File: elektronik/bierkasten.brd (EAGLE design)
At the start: 41 x 51 mm, 81 parts, among them Q1 BC547B, Q2 NXP2301P-SOT23

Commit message: Fertigungsdaten erstellt
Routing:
- net !RESET: track 52.9 -> 52.1 mm
- net GND: vias 37 -> 38
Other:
- board text added: "B.Cool v 1.0"
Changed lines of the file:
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@@
 <circle x="37.5" y="47" radius="3.2" width="0.2" layer="42"/>
 <hole x="37.5" y="47" drill="3.4"/>
+<text x="6.6" y="30.8" size="1.778" layer="1" font="vector" ratio="10">B.Cool
+v 1.0</text>
+<wire x1="13.4" y1="33.4" x2="12.2" y2="32.2" width="0.2" layer="41"/>
+<wire x1="12.2" y1="32.2" x2="12.2" y2="31.2" width="0.2" layer="41"/>
+<wire x1="12.2" y1="31.2" x2="11.8" y2="30.6" width="0.2" layer="41"/>
+<wire x1="11.8" y1="30.6" x2="11.2" y2="30.6" width="0.2" layer="41"/>
+<wire x1="11.2" y1="30.6" x2="6.4" y2="30.6" width="0.2" layer="41"/>
+<wire x1="6.4" y1="30.6" x2="6.4" y2="35.4" width="0.2" layer="41"/>
+<wire x1="6.4" y1="35.4" x2="13.4" y2="35.4" width="0.2" layer="41"/>
+<wire x1="13.4" y1="35.4" x2="13.4" y2="33.4" width="0.2" layer="41"/>
 </plain>
 <attributes>
@@
 <element name="TA1" library="switch_STE" package="TA93XX" value="KURZHUBTASTER" x="6.6" y="39.8" rot="R180">
 <attribute name="FARNELL" value="2292960" x="6.6" y="39.8" size="1.778" layer="27" rot="R180" display="off"/>
-<attribute name="REICHELT" value="Taster 9314" x="6.6" y="39.8" size="1.778" layer="27" rot="R180" display="off"/>
-<attribute name="WUERTH" value="430 182 043 816" x="6.6" y="39.8" size="1.778" layer="27" rot="R180" display="off"/>
 </element>
 <element name="U$15" library="misc_STE" package="ESP8266-POLLIN" value="ESP8266-POLLIN" x="14.8" y="18.4" rot="R90">
@@
 <attribute name="REICHELT" value="NX2301P NXP" x="12.4" y="6.4" size="1.778" layer="28" rot="MR270" display="off"/>
 </element>
-<element name="R28" library="rcl" library_urn="urn:adsk.eagle:library:334" package="R0603" package3d_urn="urn:adsk.eagle:package:23555/2" value="10k" x="14.8" y="6.4" rot="MR270">
+<element name="R28" library="rcl" library_urn="urn:adsk.eagle:library:334" package="R0603" package3d_urn="urn:adsk.eagle:package:23555/2" value="10k" x="14.8" y="6.4" smashed="yes" rot="MR270">
 <attribute name="FARNELL" value="2502397" x="14.8" y="6.4" size="1.778" layer="28" rot="MR270" display="off"/>
+<attribute name="NAME" x="14.165" y="7.035" size="1.27" layer="26" rot="MR270"/>
 <attribute name="REICHELT" value="RND 0603 1 10K" x="14.8" y="6.4" size="1.778" layer="28" rot="MR270" display="off"/>
 <attribute name="SPICEPREFIX" value="R" x="14.8" y="6.4" size="1.778" layer="28" rot="MR270" display="off"/>
+<attribute name="VALUE" x="16.705" y="7.035" size="1.27" layer="28" rot="MR270"/>
 </element>
 <element name="U$16" library="power_STE" package="SOT223" value="NCP1117ST33T3G" x="11.4" y="39" rot="MR90">
@@
 <via x="12.6" y="12.8" extent="1-16" drill="0.4"/>
 <via x="4" y="29.4" extent="1-16" drill="0.4"/>
-<via x="7" y="34.8" extent="1-16" drill="0.4"/>
+<via x="5.6" y="36.6" extent="1-16" drill="0.4"/>
 <via x="18.2" y="39.4" extent="1-16" drill="0.4"/>
-<via x="11.6" y="30.2" extent="1-16" drill="0.4"/>
+<via x="11.6" y="29.8" extent="1-16" drill="0.4"/>
 <via x="10.8" y="46.8" extent="1-16" drill="0.4"/>
-<via x="13.8" y="34" extent="1-16" drill="0.4"/>
+<via x="14.4" y="34" extent="1-16" drill="0.4"/>
 <via x="39.8" y="41.2" extent="1-16" drill="0.4"/>
 <via x="38.2" y="40.6" extent="1-16" drill="0.4"/>
@@
 <wire x1="40.45" y1="31.7" x2="34.65" y2="31.7" width="0.2" layer="16"/>
 <wire x1="40.4" y1="33.78" x2="34.6" y2="33.78" width="0.2" layer="16"/>
+<via x="9.6" y="15.2" extent="1-16" drill="0.4"/>
 </signal>
 <signal name="AVCC">
@@
 <wire x1="11.1524" y1="22.04065" x2="11.1524" y2="23.65455" width="0.2" layer="16"/>
 <wire x1="12.90455" y1="21.7976" x2="11.39545" y2="21.7976" width="0.2" layer="16"/>
-<wire x1="2.1" y1="42.05" x2="2.1" y2="42.4" width="0.2" layer="1"/>
-<wire x1="2.1" y1="42.4" x2="2.1" y2="42.5" width="0.2" layer="1"/>
 <wire x1="11.1" y1="42.05" x2="2.1" y2="42.05" width="0.2" layer="1"/>
 <wire x1="20.92" y1="42.05" x2="23.6" y2="44.73" width="0.2" layer="1"/>
@@
 <wire x1="11.6" y1="28" x2="10" y2="26.4" width="0.2" layer="16"/>
 <wire x1="10" y1="26.4" x2="10" y2="24.1976" width="0.2" layer="16"/>
-<wire x1="2.1" y1="42.05" x2="2.1" y2="42.4" width="0.2" layer="1"/>
 </signal>
 <signal name="N$1">
@@
 </drawing>
 <compatibility>
+<note version="6.3" minversion="6.2.2" severity="warning">
+Since Version 6.2.2 text objects can contain more than one line,
+which will not be processed correctly with this version.
+</note>
 <note version="8.2" severity="warning">
 Since Version 8.2, EAGLE supports online libraries. The ids

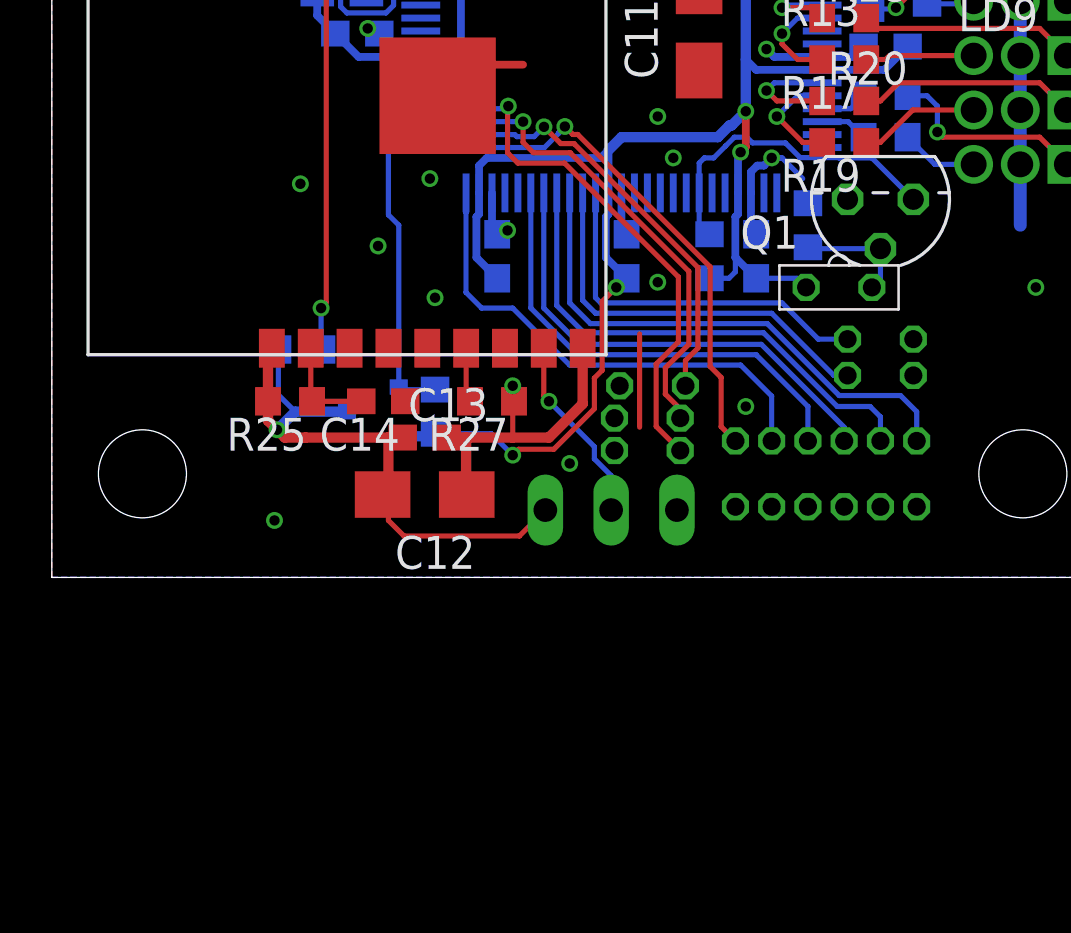
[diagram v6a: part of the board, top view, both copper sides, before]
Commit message: Light detection has its own PCB
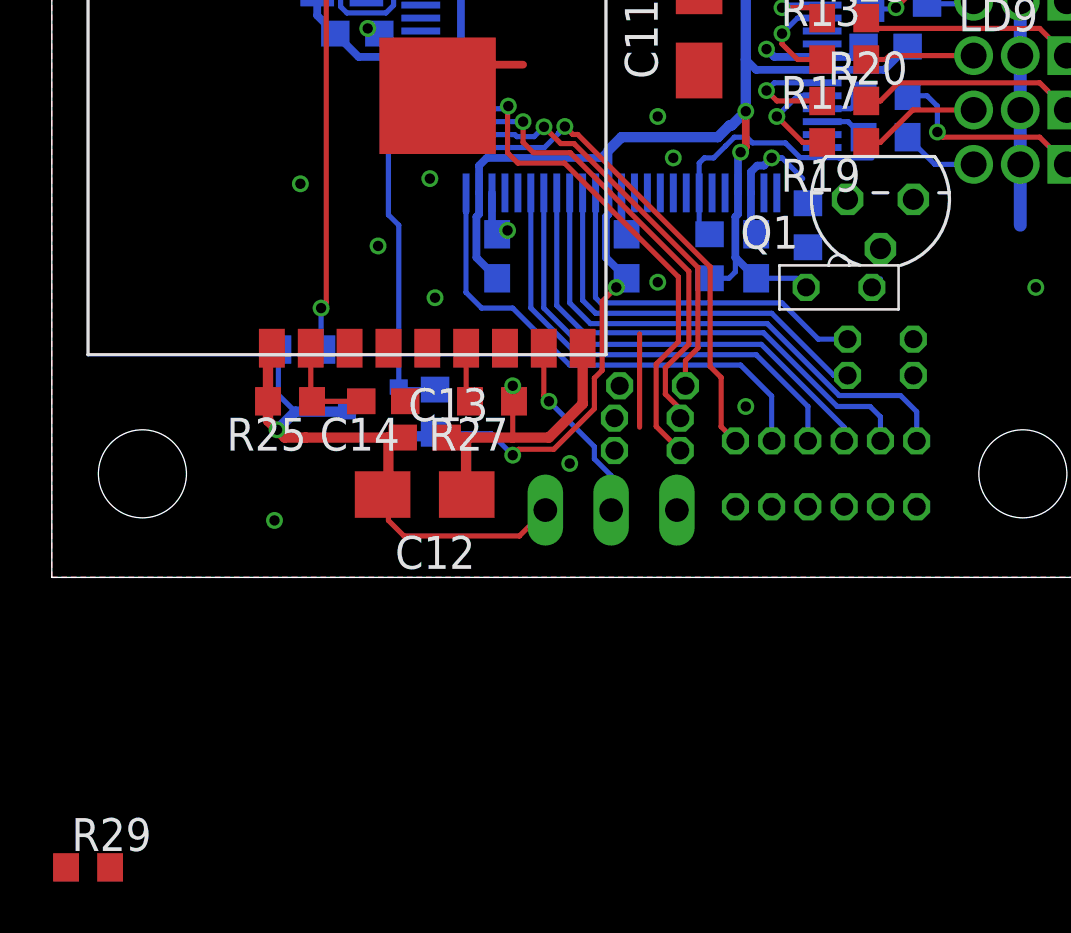
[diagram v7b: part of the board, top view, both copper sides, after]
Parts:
- added R29: 10k, rcl_STE:R0603
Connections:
- new net N$27: Q1.3
- new net N$28: Q1.2, R29.1
- net !LIGHT_ON: no longer Q1.3
- net N$23: now also R29.2; no longer Q1.2
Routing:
- net N$23: track 4.45 -> 0.54 mm
- net !LIGHT_ON: track 12.6 -> 10.3 mm
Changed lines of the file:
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@@
 <attribute name="SPICEPREFIX" value="C" x="3.4" y="39" size="1.778" layer="28" rot="MR90" display="off"/>
+</element>
+<element name="R29" library="rcl_STE" package="R0603" package3d_urn="urn:adsk.eagle:package:23555/2" value="10k" x="1.4" y="-11.2">
+<attribute name="REICHELT" value="RND 0603 1 1,0M" x="1.4" y="-11.2" size="1.778" layer="27" display="off"/>
+<attribute name="SPICEPREFIX" value="R" x="1.4" y="-11.2" size="1.778" layer="27" display="off"/>
 </element>
 </elements>
@@
 <contactref element="U$2" pad="4"/>
 <contactref element="R24" pad="2"/>
-<contactref element="U$3" pad="C"/>
 <wire x1="29.75" y1="24.6" x2="32.05" y2="24.6" width="0.3" layer="16"/>
 <wire x1="32.05" y1="24.6" x2="33.05" y2="25.6" width="0.3" layer="16"/>
@@
 <wire x1="26.3976" y1="11.7976" x2="26.15" y2="11.55" width="0.2" layer="16"/>
 <wire x1="27.2" y1="11.55" x2="28.78" y2="11.55" width="0.2" layer="16"/>
-<wire x1="28.78" y1="11.55" x2="29.13" y2="11.2" width="0.2" layer="16"/>
 <wire x1="10.625" y1="32.2" x2="10.45" y2="32.375" width="1" layer="16"/>
 <wire x1="10.45" y1="32.375" x2="10.45" y2="34.4" width="1" layer="16"/>
@@
 <wire x1="26.14" y1="42.0406" x2="26.14" y2="41.74" width="0.2" layer="1"/>
 <wire x1="24.6" y1="40.2" x2="30.8" y2="40.2" width="0.2" layer="1"/>
+<contactref element="U$3" pad="C"/>
+<wire x1="15" y1="36.2" x2="14.55" y2="39" width="0" layer="19" extent="16-16"/>
+<wire x1="21.8" y1="33.65" x2="20.4" y2="36.8" width="0" layer="19" extent="1-16"/>
+<wire x1="29.13" y1="11.2" x2="28.78" y2="11.55" width="0" layer="19" extent="16-16"/>
 </signal>
 <signal name="GND">
@@
 <contactref element="U$3" pad="E"/>
 <contactref element="R23" pad="2"/>
-<contactref element="Q1" pad="2"/>
-<wire x1="32" y1="12.695" x2="29.255" y2="12.695" width="0.2" layer="16"/>
 <wire x1="29.255" y1="12.695" x2="29.2" y2="12.75" width="0.2" layer="16"/>
-<wire x1="32" y1="12.695" x2="32" y2="11.53" width="0.2" layer="16"/>
 <wire x1="32" y1="11.53" x2="31.67" y2="11.2" width="0.2" layer="16"/>
+<contactref element="R29" pad="2"/>
+<wire x1="29.255" y1="12.695" x2="31.67" y2="11.2" width="0" layer="19" extent="16-16"/>
+<wire x1="2.25" y1="-11.2" x2="29.2" y2="12.75" width="0" layer="19" extent="1-16"/>
 </signal>
 <signal name="!LIGHT_ON">
 <contactref element="U$1" pad="57"/>
-<contactref element="Q1" pad="3"/>
 <contactref element="R24" pad="1"/>
 <wire x1="25" y1="14.85" x2="25" y2="13.65" width="0.2" layer="16"/>
@@
 <wire x1="30.4024" y1="16.1976" x2="31.6724" y2="16.1976" width="0.2" layer="16"/>
 <wire x1="27.0606" y1="16.7794" x2="28.32865" y2="16.7794" width="0.2" layer="16"/>
-<wire x1="31.6724" y1="16.1976" x2="33.27" y2="14.6" width="0.2" layer="16"/>
 </signal>
 <signal name="SWITCH_0">
@@
 <wire x1="2.425" y1="40.625" x2="1.8" y2="40" width="1" layer="16"/>
 </signal>
+<signal name="N$27">
+<contactref element="Q1" pad="3"/>
+</signal>
+<signal name="N$28">
+<contactref element="Q1" pad="2"/>
+<contactref element="R29" pad="1"/>
+<wire x1="0.55" y1="-11.2" x2="32" y2="12.695" width="0" layer="19" extent="1-1"/>
+</signal>
 </signals>
